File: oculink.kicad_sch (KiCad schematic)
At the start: 19 parts, among them J6 OCuLink_x4_Amphenol_G14A42121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

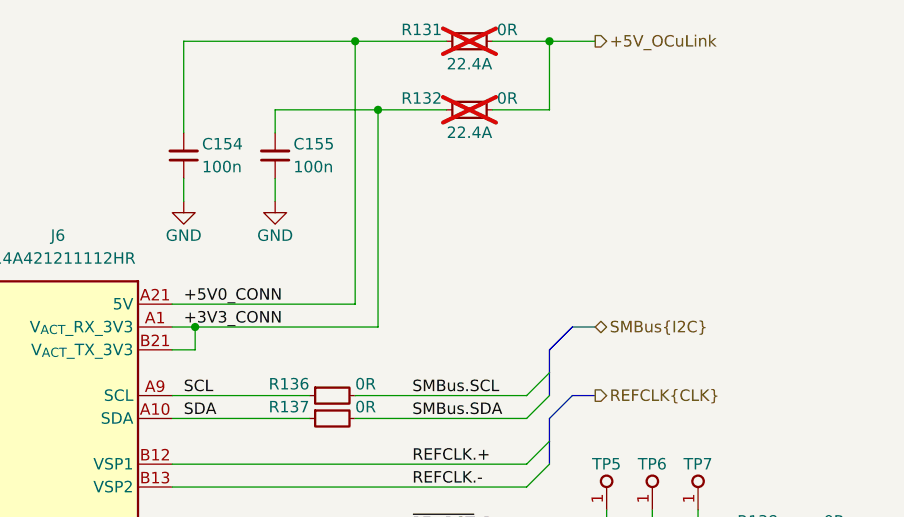
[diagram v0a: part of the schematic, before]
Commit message: [#80813] Remove OCuLink power pins connections
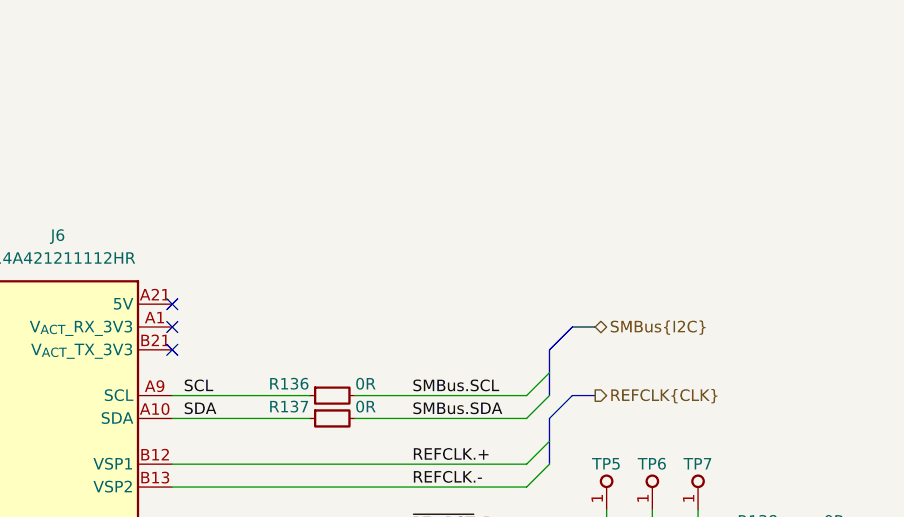
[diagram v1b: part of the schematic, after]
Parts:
- removed C154, C155: C_100n_16V_X7R_0402, antmicro-footprints:C_0402_1005Metric, symbol antmicroCapacitors0402:C_100n_16V_X7R_0402
- removed R131, R132: R_0R_22.4A_0603, antmicro-footprints:R_0603_1608Metric, symbol antmicroResistors0603:R_0R_22.4A_0603
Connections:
- net +3V3_CONN: no longer names the net of J6.A1 (V_{ACT}_RX_3V3)
- net +3V3_CONN: no longer J6.B21 (V_{ACT}_TX_3V3)
- net +5V0_CONN: no longer names the net of J6.A21 (5V), J6.B1 (5V)
- no-connect marks 2 -> 5

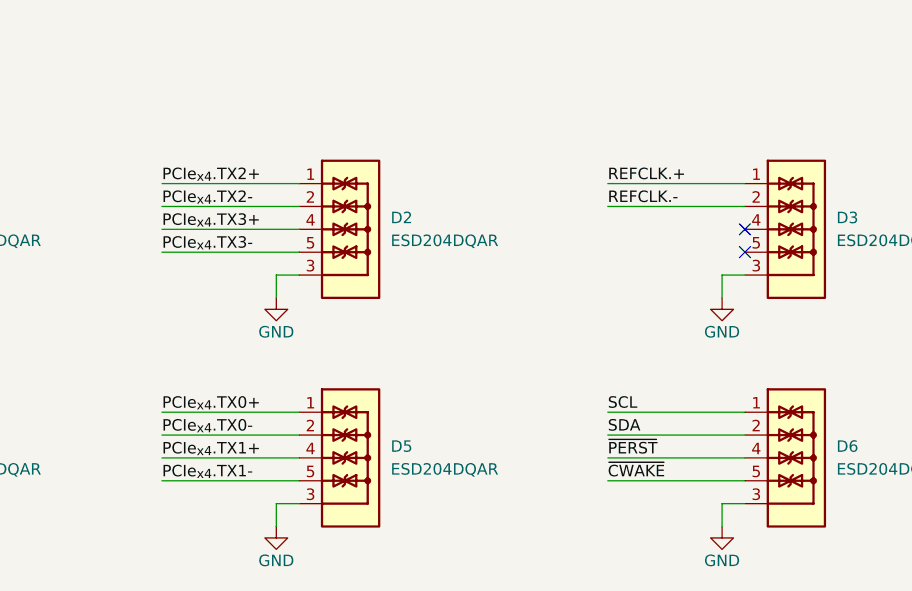
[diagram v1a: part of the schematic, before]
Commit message: [#80813] Change inductors, minor PCB changes
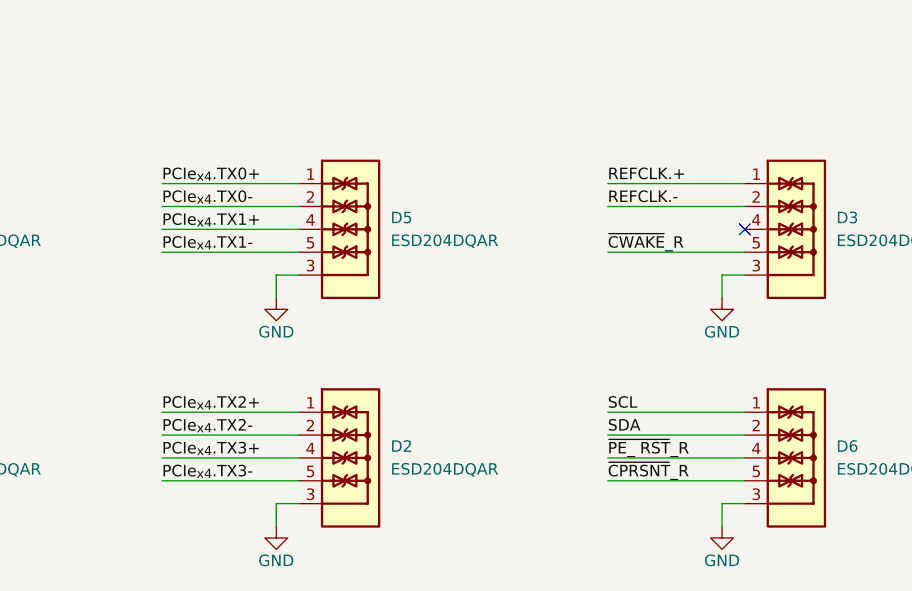
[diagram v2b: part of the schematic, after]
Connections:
- net ~{CWAKE} is gone; now on net ~{CPRSNT}_R: D6.5, D6.6
- net ~{PERST} is gone; now on net ~{PE_ RST}_R: D6.4, D6.7
- net ~{CWAKE}_R: now also D3.5, D3.6
- no-connect marks 5 -> 4
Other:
- moved on the sheet: D2, D5
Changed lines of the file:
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@@
 	)
 	(no_connect
-		(at 261.62 217.17)
-	)
-	(no_connect
 		(at 191.77 87.63)
 	)
@@
 	(wire
 		(pts
-			(xy 212.09 242.57) (xy 196.85 242.57)
+			(xy 212.09 217.17) (xy 196.85 217.17)
 		)
 		(stroke
@@
 	(wire
 		(pts
-			(xy 209.55 219.71) (xy 212.09 219.71)
+			(xy 209.55 245.11) (xy 212.09 245.11)
 		)
 		(stroke
@@
 	(wire
 		(pts
-			(xy 209.55 219.71) (xy 209.55 222.25)
+			(xy 209.55 245.11) (xy 209.55 247.65)
 		)
 		(stroke
@@
 	(wire
 		(pts
-			(xy 212.09 212.09) (xy 196.85 212.09)
+			(xy 212.09 237.49) (xy 196.85 237.49)
 		)
 		(stroke
@@
 	(wire
 		(pts
-			(xy 212.09 217.17) (xy 196.85 217.17)
+			(xy 212.09 242.57) (xy 196.85 242.57)
 		)
 		(stroke
@@
 	(wire
 		(pts
-			(xy 212.09 214.63) (xy 196.85 214.63)
+			(xy 212.09 240.03) (xy 196.85 240.03)
+		)
+		(stroke
+			(width 0)
+			(type default)
+		)
+	)
+	(wire
+		(pts
+			(xy 246.38 217.17) (xy 261.62 217.17)
 		)
 		(stroke
@@
 	(wire
 		(pts
-			(xy 212.09 209.55) (xy 196.85 209.55)
+			(xy 212.09 234.95) (xy 196.85 234.95)
 		)
 		(stroke
@@
 	(wire
 		(pts
-			(xy 212.09 234.95) (xy 196.85 234.95)
+			(xy 212.09 209.55) (xy 196.85 209.55)
 		)
 		(stroke
@@
 	(wire
 		(pts
-			(xy 212.09 240.03) (xy 196.85 240.03)
+			(xy 212.09 214.63) (xy 196.85 214.63)
 		)
 		(stroke
@@
 	(wire
 		(pts
-			(xy 209.55 245.11) (xy 212.09 245.11)
+			(xy 209.55 219.71) (xy 212.09 219.71)
 		)
 		(stroke
@@
 	(wire
 		(pts
-			(xy 209.55 245.11) (xy 209.55 247.65)
+			(xy 209.55 219.71) (xy 209.55 222.25)
 		)
 		(stroke
@@
 	(wire
 		(pts
-			(xy 212.09 237.49) (xy 196.85 237.49)
+			(xy 212.09 212.09) (xy 196.85 212.09)
 		)
 		(stroke
@@
 		)
 	)
-	(label "~{CWAKE}"
-		(at 246.38 242.57 0)
+	(label "~{PE_ RST}_R"
+		(at 246.38 240.03 0)
 		(effects
 			(font
@@
 	)
 	(label "PCIe_{x4}.TX1-"
-		(at 196.85 242.57 0)
+		(at 196.85 217.17 0)
 		(effects
 			(font
@@
 		)
 	)
+	(label "~{CWAKE}_R"
+		(at 246.38 217.17 0)
+		(effects
+			(font
+				(size 1.27 1.27)
+			)
+			(justify left bottom)
+		)
+	)
 	(label "PCIe_{x4}.RX1-"
 		(at 146.05 217.17 0)
@@
 	)
 	(label "PCIe_{x4}.TX0+"
-		(at 196.85 234.95 0)
+		(at 196.85 209.55 0)
+		(effects
+			(font
+				(size 1.27 1.27)
+			)
+			(justify left bottom)
+		)
+	)
+	(label "~{CPRSNT}_R"
+		(at 246.38 242.57 0)
 		(effects
 			(font
@@
 	)
 	(label "PCIe_{x4}.TX2+"
-		(at 196.85 209.55 0)
+		(at 196.85 234.95 0)
 		(effects
 			(font
@@
 	)
 	(label "PCIe_{x4}.TX3+"
-		(at 196.85 214.63 0)
+		(at 196.85 240.03 0)
 		(effects
 			(font
@@
 	)
 	(label "PCIe_{x4}.TX0-"
-		(at 196.85 237.49 0)
+		(at 196.85 212.09 0)
 		(effects
 			(font
@@
 	)
 	(label "PCIe_{x4}.TX3-"
-		(at 196.85 217.17 0)
+		(at 196.85 242.57 0)
 		(effects
 			(font
@@
 	)
 	(label "PCIe_{x4}.TX1+"
-		(at 196.85 240.03 0)
+		(at 196.85 214.63 0)
 		(effects
 			(font
@@
 	)
 	(label "PCIe_{x4}.TX2-"
-		(at 196.85 212.09 0)
+		(at 196.85 237.49 0)
 		(effects
 			(font
@@
 		)
 	)
-	(label "~{PERST}"
-		(at 246.38 240.03 0)
-		(effects
-			(font
-				(size 1.27 1.27)
-			)
-			(justify left bottom)
-		)
-	)
 	(label "~{CWAKE}_R"
 		(at 218.44 115.57 0)
@@
 	(symbol
 		(lib_id "antmicroTVSDiodes:ESD204DQAR")
-		(at 212.09 209.55 0)
+		(at 212.09 234.95 0)
 		(unit 1)
 		(exclude_from_sim no)
@@
 		(fields_autoplaced yes)
 		(property "Reference" "D2"
-			(at 222.25 213.36 0)
+			(at 222.25 238.76 0)
 			(effects
 				(font
@@
 		)
 		(property "Value" "ESD204DQAR"
-			(at 236.22 214.63 0)
+			(at 236.22 240.03 0)
 			(effects
 				(font
@@
 		)
 		(property "Footprint" "antmicro-footprints:USON-10_2.5x1mm_P0.5mm"
-			(at 236.22 217.17 0)
+			(at 236.22 242.57 0)
 			(effects
 				(font
@@
 		)
 		(property "Datasheet" "https://www.ti.com/lit/ds/symlink/esd204.pdf?ts=1706004844383&ref_url=https%253A%252F%252Fwww.ti.com%252Finterface%252Fdiodes%252Fesd-protection-diodes%252Fproducts.html"
-			(at 236.22 219.71 0)
+			(at 236.22 245.11 0)
 			(effects
 				(font
@@
 		)
 		(property "Description" "TVS diode array, 30 kV, USON-10, 3.6 V, 0.55 pF"
-			(at 236.22 229.87 0)
+			(at 236.22 255.27 0)
 			(effects
 				(font
@@
 		)
 		(property "MPN" "ESD204DQAR"
-			(at 222.25 215.9 0)
+			(at 222.25 241.3 0)
 			(effects
 				(font
@@
 		)
 		(property "Manufacturer" "Texas Instruments"
-			(at 236.22 222.25 0)
+			(at 236.22 247.65 0)
 			(effects
 				(font
@@
 		)
 		(property "Author" "Antmicro"
-			(at 236.22 224.79 0)
+			(at 236.22 250.19 0)
 			(effects
 				(font
@@
 		)
 		(property "License" "Apache-2.0"
-			(at 236.22 227.33 0)
+			(at 236.22 252.73 0)
 			(effects
 				(font
@@
 	(symbol
 		(lib_id "antmicroTVSDiodes:ESD204DQAR")
-		(at 212.09 234.95 0)
+		(at 212.09 209.55 0)
 		(unit 1)
 		(exclude_from_sim no)
@@
 		(fields_autoplaced yes)
 		(property "Reference" "D5"
-			(at 222.25 238.76 0)
+			(at 222.25 213.36 0)
 			(effects
 				(font
@@
 		)
 		(property "Value" "ESD204DQAR"
-			(at 236.22 240.03 0)
+			(at 236.22 214.63 0)
 			(effects
 				(font
@@
 		)
 		(property "Footprint" "antmicro-footprints:USON-10_2.5x1mm_P0.5mm"
-			(at 236.22 242.57 0)
+			(at 236.22 217.17 0)
 			(effects
 				(font
@@
 		)
 		(property "Datasheet" "https://www.ti.com/lit/ds/symlink/esd204.pdf?ts=1706004844383&ref_url=https%253A%252F%252Fwww.ti.com%252Finterface%252Fdiodes%252Fesd-protection-diodes%252Fproducts.html"
-			(at 236.22 245.11 0)
+			(at 236.22 219.71 0)
 			(effects
 				(font
@@
 		)
 		(property "Description" "TVS diode array, 30 kV, USON-10, 3.6 V, 0.55 pF"
-			(at 236.22 255.27 0)
+			(at 236.22 229.87 0)
 			(effects
 				(font
@@
 		)
 		(property "MPN" "ESD204DQAR"
-			(at 222.25 241.3 0)
+			(at 222.25 215.9 0)
 			(effects
 				(font
@@
 		)
 		(property "Manufacturer" "Texas Instruments"
-			(at 236.22 247.65 0)
+			(at 236.22 222.25 0)
 			(effects
 				(font
@@
 		)
 		(property "Author" "Antmicro"
-			(at 236.22 250.19 0)
+			(at 236.22 224.79 0)
 			(effects
 				(font
@@
 		)
 		(property "License" "Apache-2.0"
-			(at 236.22 252.73 0)
+			(at 236.22 227.33 0)
 			(effects
 				(font
@@
 	(symbol
 		(lib_id "antmicropower:GND")
-		(at 209.55 222.25 0)
+		(at 209.55 247.65 0)
 		(unit 1)
 		(exclude_from_sim no)
@@
 		(dnp no)
 		(property "Reference" "#PWR0269"
-			(at 218.44 224.79 0)
+			(at 218.44 250.19 0)
 			(effects
 				(font
@@
 		)
 		(property "Value" "GND"
-			(at 209.55 226.06 0)
+			(at 209.55 251.46 0)
 			(effects
 				(font
@@
 		)
 		(property "Footprint" ""
-			(at 218.44 229.87 0)
+			(at 218.44 255.27 0)
 			(effects
 				(font
@@
 		)
 		(property "Datasheet" ""
-			(at 218.44 234.95 0)
+			(at 218.44 260.35 0)
 			(effects
 				(font
@@
 		)
 		(property "Description" ""
-			(at 209.55 222.25 0)
+			(at 209.55 247.65 0)
 			(effects
 				(font
@@
 		)
 		(property "Author" "Antmicro"
-			(at 218.44 229.87 0)
+			(at 218.44 255.27 0)
 			(effects
 				(font
@@
 		)
 		(property "License" "Apache-2.0"
-			(at 218.44 232.41 0)
+			(at 218.44 257.81 0)
 			(effects
 				(font
@@
 	(symbol
 		(lib_id "antmicropower:GND")
-		(at 209.55 247.65 0)
+		(at 209.55 222.25 0)
 		(unit 1)
 		(exclude_from_sim no)
@@
 		(dnp no)
 		(property "Reference" "#PWR0273"
-			(at 218.44 250.19 0)
+			(at 218.44 224.79 0)
 			(effects
 				(font
@@
 		)
 		(property "Value" "GND"
-			(at 209.55 251.46 0)
+			(at 209.55 226.06 0)
 			(effects
 				(font
@@
 		)
 		(property "Footprint" ""
-			(at 218.44 255.27 0)
+			(at 218.44 229.87 0)
 			(effects
 				(font
@@
 		)
 		(property "Datasheet" ""
-			(at 218.44 260.35 0)
+			(at 218.44 234.95 0)
 			(effects
 				(font
@@
 		)
 		(property "Description" ""
-			(at 209.55 247.65 0)
+			(at 209.55 222.25 0)
 			(effects
 				(font
@@
 		)
 		(property "Author" "Antmicro"
-			(at 218.44 255.27 0)
+			(at 218.44 229.87 0)
 			(effects
 				(font
@@
 		)
 		(property "License" "Apache-2.0"
-			(at 218.44 257.81 0)
+			(at 218.44 232.41 0)
 			(effects
 				(font
